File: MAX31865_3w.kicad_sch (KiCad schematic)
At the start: 6 parts, among them J1 Screw_Terminal_01x03, U3 MAX31865xAP

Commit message: Supprime le contour arduino qui fait plein d'erreur DRC
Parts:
- J1: footprint (none) -> TerminalBlock_Phoenix:TerminalBlock_Phoenix_MPT-0,5-3-2.54_1x03_P2.54mm_Horizontal
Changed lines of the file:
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@@
       (effects (font (size 1.27 1.27)) (justify left))
     )
-    (property "Footprint" "" (id 2) (at 212.09 90.17 0)
+    (property "Footprint" "TerminalBlock_Phoenix:TerminalBlock_Phoenix_MPT-0,5-3-2.54_1x03_P2.54mm_Horizontal" (id 2) (at 212.09 90.17 0)
       (effects (font (size 1.27 1.27)) hide)
     )

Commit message: 0 DRC
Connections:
- net DRDY: no longer names the net of U3.1 (~{DRDY})
- no-connect marks 0 -> 1
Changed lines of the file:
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@@
   (junction (at 144.78 100.33) (diameter 0) (color 0 0 0 0)
   )
+  (no_connect (at 74.93 72.39))
   (wire (pts (xy 120.65 55.88) (xy 120.65 48.26))
     (stroke (width 0) (type default) (color 0 0 0 0))
@@
   )
   (wire (pts (xy 124.46 114.3) (xy 124.46 118.11))
-    (stroke (width 0) (type default) (color 0 0 0 0))
-  )
-  (wire (pts (xy 74.93 72.39) (xy 109.22 72.39))
     (stroke (width 0) (type default) (color 0 0 0 0))
   )
@@
     (stroke (width 0) (type default) (color 0 0 0 0))
   )
+  (wire (pts (xy 74.93 72.39) (xy 109.22 72.39))
+    (stroke (width 0) (type default) (color 0 0 0 0))
+  )
   (wire (pts (xy 128.27 55.88) (xy 133.35 55.88))
     (stroke (width 0) (type default) (color 0 0 0 0))
@@
     (stroke (width 0) (type default) (color 0 0 0 0))
   )
-  (hierarchical_label "DRDY" (shape output) (at 74.93 72.39 180)
-    (effects (font (size 1.27 1.27)) (justify right))
-  )
   (hierarchical_label "SCLK" (shape input) (at 74.93 77.47 180)

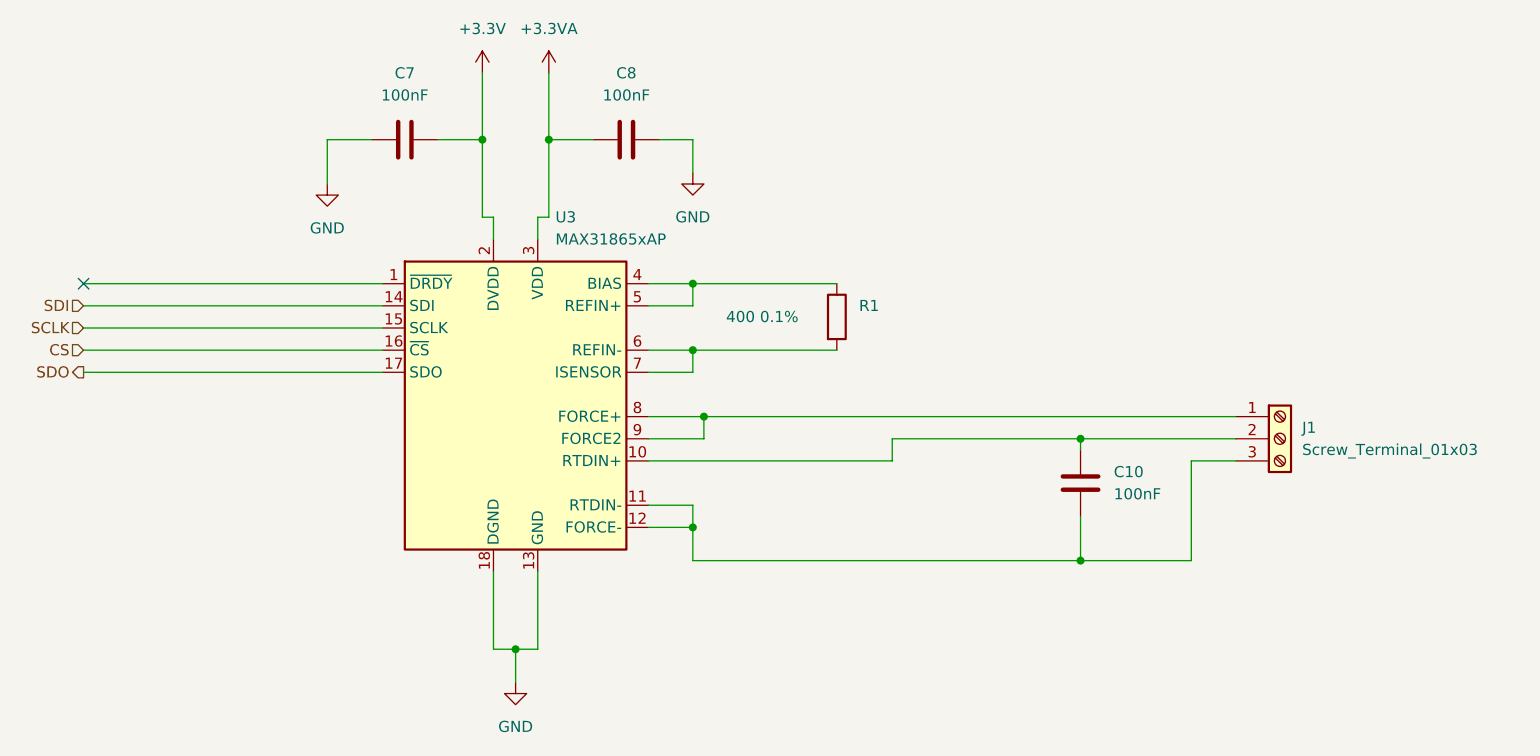
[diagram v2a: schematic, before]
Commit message: Passe l'empreinte en TSOP
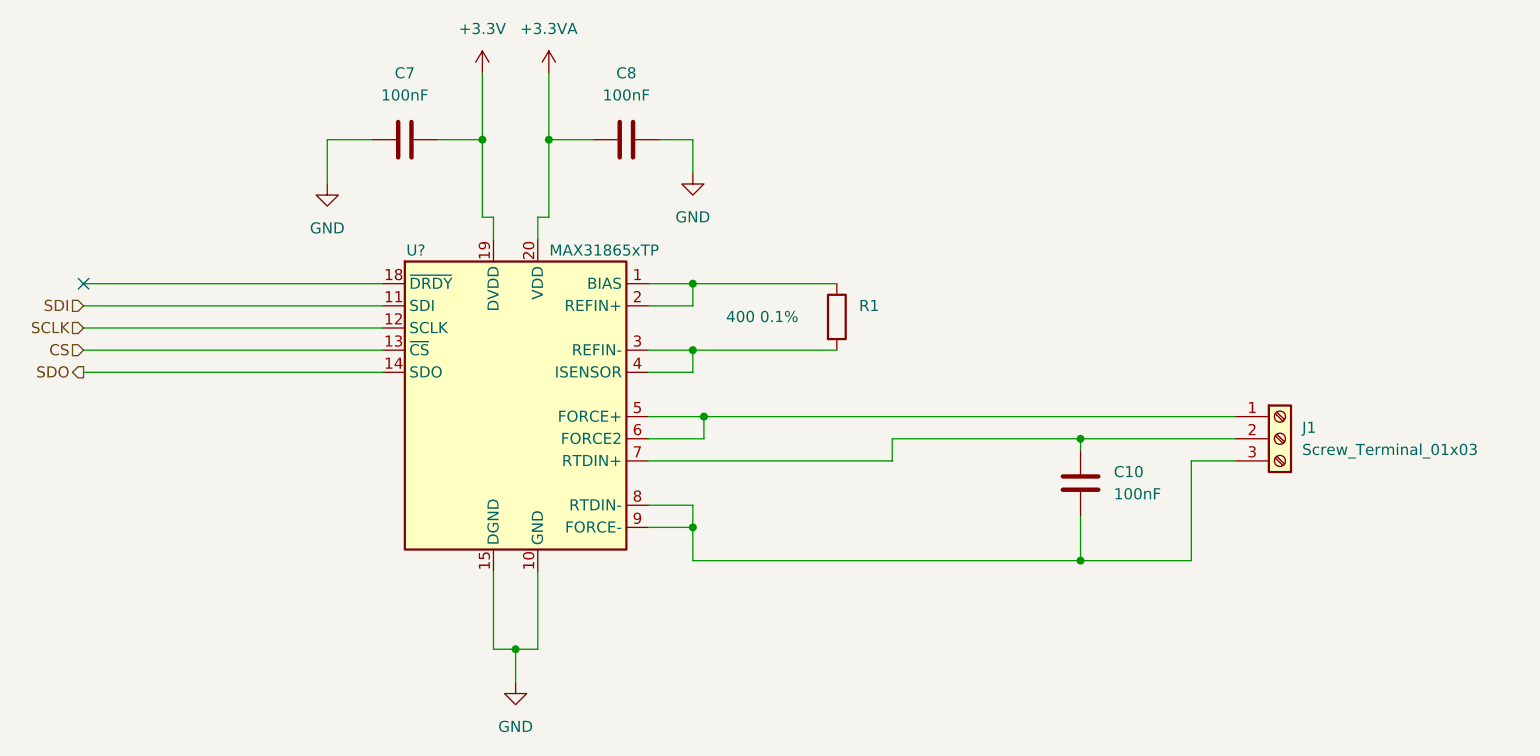
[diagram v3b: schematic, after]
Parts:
- U?: renamed from U3; value MAX31865xAP -> MAX31865xTP; footprint Package_SO:SSOP-20_5.3x7.2mm_P0.65mm -> Package_DFN_QFN:TQFN-20-1EP_5x5mm_P0.65mm_EP3.25x3.25mm; symbol Sensor_Temperature:MAX31865xAP -> Sensor_Temperature:MAX31865xTP
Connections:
- net +3.3V: now also U?.19 (DVDD); no longer U?.2 (DVDD)
- net +3.3VA: now also U?.20 (VDD); no longer U?.3 (VDD)
- net CS: now also U?.13 (~{CS}); no longer U?.16 (~{CS})
- net GND: now also U?.10 (GND), U?.15 (DGND), U?.16 (GND), U?.21 (GND); no longer U?.13 (GND), U?.18 (DGND), U?.19 (GND)
- net SCLK: now also U?.12 (SCLK); no longer U?.15 (SCLK)
- net SDI: now also U?.11 (SDI); no longer U?.14 (SDI)
- net SDO: now also U?.14 (SDO); no longer U?.17 (SDO)
- net at U?.1 (BIAS): now also R1.1, U?.2 (REFIN+)
- net at C10.2, J1.2 (Pin_2): now also U?.7 (RTDIN+); no longer U?.10 (RTDIN+)
- net at C10.1, J1.3 (Pin_3): now also U?.8 (RTDIN-), U?.9 (FORCE-); no longer U?.11 (RTDIN-), U?.12 (FORCE-)
- new net: R1.2, U?.3 (REFIN-), U?.4 (ISENSOR)
- new net: J1.1 (Pin_1), U?.5 (FORCE+), U?.6 (FORCE2)
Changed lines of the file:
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@@
     (effects (font (size 1.27 1.27)) (justify right))
   )
-  (symbol (lib_id "Sensor_Temperature:MAX31865xAP") (at 124.46 87.63 0) (unit 1)
+  (symbol (lib_id "Sensor_Temperature:MAX31865xTP") (at 124.46 87.63 0) (unit 1)
     (in_bom yes) (on_board yes) (fields_autoplaced)
-    (property "Reference" "U3" (id 0) (at 129.0194 64.77 0)
-      (effects (font (size 1.27 1.27)) (justify left))
-    )
-    (property "Value" "MAX31865xAP" (id 1) (at 129.0194 67.31 0)
-      (effects (font (size 1.27 1.27)) (justify left))
-    )
-    (property "Footprint" "Package_SO:SSOP-20_5.3x7.2mm_P0.65mm" (id 2) (at 128.27 104.14 0)
+    (property "Reference" "U?" (id 0) (at 113.03 68.58 0))
+    (property "Value" "MAX31865xTP" (id 1) (at 134.62 68.58 0))
+    (property "Footprint" "Package_DFN_QFN:TQFN-20-1EP_5x5mm_P0.65mm_EP3.25x3.25mm" (id 2) (at 128.27 104.14 0)
       (effects (font (size 1.27 1.27)) (justify left) hide)
     )
@@
     (pin "2")
     (pin "20")
+    (pin "21")
     (pin "3")
     (pin "4")

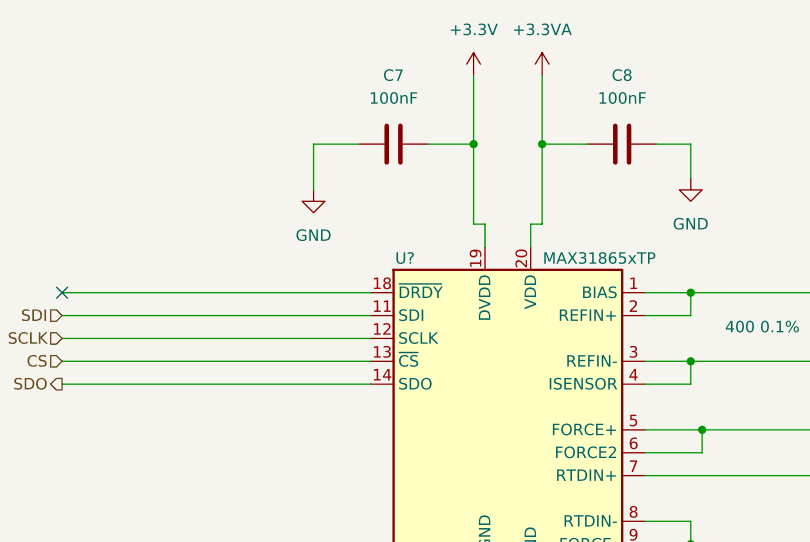
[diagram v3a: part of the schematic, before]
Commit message: Passe l'empreinte en TSOP
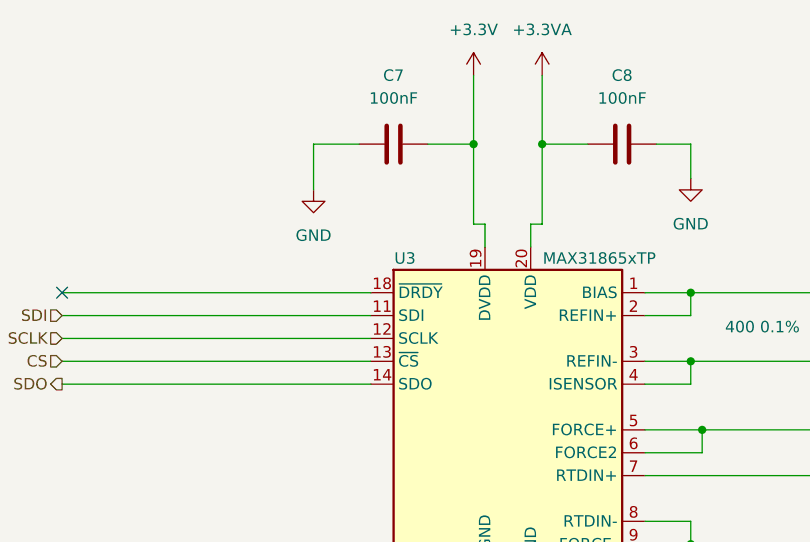
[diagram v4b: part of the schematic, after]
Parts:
- gave numbers to parts that had none: 1
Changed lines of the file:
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@@
   (symbol (lib_id "Sensor_Temperature:MAX31865xTP") (at 124.46 87.63 0) (unit 1)
     (in_bom yes) (on_board yes) (fields_autoplaced)
-    (property "Reference" "U?" (id 0) (at 113.03 68.58 0))
+    (property "Reference" "U3" (id 0) (at 113.03 68.58 0))
     (property "Value" "MAX31865xTP" (id 1) (at 134.62 68.58 0))
     (property "Footprint" "Package_DFN_QFN:TQFN-20-1EP_5x5mm_P0.65mm_EP3.25x3.25mm" (id 2) (at 128.27 104.14 0)

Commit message: Passe certaine empreinte en 0603
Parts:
- C10, C7, C8: footprint Capacitor_SMD:C_0805_2012Metric_Pad1.18x1.45mm_HandSolder -> Capacitor_SMD:C_0603_1608Metric_Pad1.08x0.95mm_HandSolder
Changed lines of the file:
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@@
     (property "Reference" "C7" (id 0) (at 111.76 48.26 90))
     (property "Value" "100nF" (id 1) (at 111.76 50.8 90))
-    (property "Footprint" "Capacitor_SMD:C_0805_2012Metric_Pad1.18x1.45mm_HandSolder" (id 2) (at 115.57 54.9148 0)
+    (property "Footprint" "Capacitor_SMD:C_0603_1608Metric_Pad1.08x0.95mm_HandSolder" (id 2) (at 115.57 54.9148 0)
       (effects (font (size 1.27 1.27)) hide)
     )
@@
     (property "Reference" "C8" (id 0) (at 137.16 48.26 90))
     (property "Value" "100nF" (id 1) (at 137.16 50.8 90))
-    (property "Footprint" "Capacitor_SMD:C_0805_2012Metric_Pad1.18x1.45mm_HandSolder" (id 2) (at 140.97 54.9148 0)
+    (property "Footprint" "Capacitor_SMD:C_0603_1608Metric_Pad1.08x0.95mm_HandSolder" (id 2) (at 140.97 54.9148 0)
       (effects (font (size 1.27 1.27)) hide)
     )
@@
       (effects (font (size 1.27 1.27)) (justify right))
     )
-    (property "Footprint" "Capacitor_SMD:C_0805_2012Metric_Pad1.18x1.45mm_HandSolder" (id 2) (at 188.2648 91.44 0)
+    (property "Footprint" "Capacitor_SMD:C_0603_1608Metric_Pad1.08x0.95mm_HandSolder" (id 2) (at 188.2648 91.44 0)
       (effects (font (size 1.27 1.27)) hide)
     )

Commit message: Passe les resistance 400 ohm en 1206
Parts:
- R1: footprint Resistor_SMD:R_0805_2012Metric_Pad1.20x1.40mm_HandSolder -> Resistor_SMD:R_1206_3216Metric_Pad1.30x1.75mm_HandSolder
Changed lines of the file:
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@@
       (effects (font (size 1.27 1.27)) (justify left))
     )
-    (property "Footprint" "Resistor_SMD:R_0805_2012Metric_Pad1.20x1.40mm_HandSolder" (id 2) (at 159.512 76.2 90)
+    (property "Footprint" "Resistor_SMD:R_1206_3216Metric_Pad1.30x1.75mm_HandSolder" (id 2) (at 159.512 76.2 90)
       (effects (font (size 1.27 1.27)) hide)
     )

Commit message: Ajoute selection 4w/3w Ajoute marquage v002
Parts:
- removed J1: Screw_Terminal_01x03, TerminalBlock_Phoenix:TerminalBlock_Phoenix_MPT-0,5-3-2.54_1x03_P2.54mm_Horizontal, symbol Connector:Screw_Terminal_01x03
- added J1: Screw_Terminal_01x04, TerminalBlock_Phoenix:TerminalBlock_Phoenix_MPT-0,5-4-2.54_1x04_P2.54mm_Horizontal, symbol Connector:Screw_Terminal_01x04
- added JP13, JP14: SolderJumper_3_Open, Jumper:SolderJumper-3_P1.3mm_Open_RoundedPad1.0x1.5mm_NumberLabels, symbol Jumper:SolderJumper_3_Open
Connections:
- net GND: now also JP13.3 (B)
- net at U3.5 (FORCE+): now also J1.1 (Pin_1), JP13.1 (A); no longer U3.6 (FORCE2)
- net at C10.2, U3.7 (RTDIN+): now also J1.2 (Pin_2)
- net at C10.1, U3.8 (RTDIN-): now also J1.3 (Pin_3), JP14.1 (A); no longer U3.9 (FORCE-)
- new net: JP13.2 (C), U3.6 (FORCE2)
- new net: JP14.2 (C), U3.9 (FORCE-)
- new net: J1.4 (Pin_4), JP14.3 (B)
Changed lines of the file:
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@@
   (junction (at 144.78 72.39) (diameter 0) (color 0 0 0 0)
   )
+  (junction (at 189.23 104.14) (diameter 0) (color 0 0 0 0)
+  )
   (junction (at 144.78 80.01) (diameter 0) (color 0 0 0 0)
   )
-  (junction (at 189.23 104.14) (diameter 0) (color 0 0 0 0)
+  (junction (at 142.24 87.63) (diameter 0) (color 0 0 0 0)
   )
   (junction (at 124.46 114.3) (diameter 0) (color 0 0 0 0)
   )
-  (junction (at 146.05 87.63) (diameter 0) (color 0 0 0 0)
-  )
   (junction (at 189.23 90.17) (diameter 0) (color 0 0 0 0)
   )
-  (junction (at 144.78 100.33) (diameter 0) (color 0 0 0 0)
+  (junction (at 147.32 97.79) (diameter 0) (color 0 0 0 0)
   )
   (no_connect (at 74.93 72.39))
@@
     (stroke (width 0) (type default) (color 0 0 0 0))
   )
-  (wire (pts (xy 146.05 87.63) (xy 146.05 90.17))
-    (stroke (width 0) (type default) (color 0 0 0 0))
-  )
-  (wire (pts (xy 146.05 87.63) (xy 207.01 87.63))
-    (stroke (width 0) (type default) (color 0 0 0 0))
-  )
   (wire (pts (xy 189.23 104.14) (xy 201.93 104.14))
     (stroke (width 0) (type default) (color 0 0 0 0))
   )
-  (wire (pts (xy 139.7 87.63) (xy 146.05 87.63))
+  (wire (pts (xy 147.32 95.25) (xy 147.32 97.79))
     (stroke (width 0) (type default) (color 0 0 0 0))
   )
@@
     (stroke (width 0) (type default) (color 0 0 0 0))
   )
+  (wire (pts (xy 147.32 104.14) (xy 189.23 104.14))
+    (stroke (width 0) (type default) (color 0 0 0 0))
+  )
   (wire (pts (xy 121.92 114.3) (xy 124.46 114.3))
     (stroke (width 0) (type default) (color 0 0 0 0))
@@
     (stroke (width 0) (type default) (color 0 0 0 0))
   )
+  (wire (pts (xy 139.7 100.33) (xy 149.86 100.33))
+    (stroke (width 0) (type default) (color 0 0 0 0))
+  )
+  (wire (pts (xy 144.78 85.09) (xy 142.24 85.09))
+    (stroke (width 0) (type default) (color 0 0 0 0))
+  )
   (wire (pts (xy 128.27 48.26) (xy 128.27 55.88))
     (stroke (width 0) (type default) (color 0 0 0 0))
   )
+  (wire (pts (xy 204.47 95.25) (xy 207.01 95.25))
+    (stroke (width 0) (type default) (color 0 0 0 0))
+  )
   (wire (pts (xy 167.64 92.71) (xy 167.64 90.17))
     (stroke (width 0) (type default) (color 0 0 0 0))
   )
+  (wire (pts (xy 147.32 95.25) (xy 153.67 95.25))
+    (stroke (width 0) (type default) (color 0 0 0 0))
+  )
   (wire (pts (xy 74.93 77.47) (xy 109.22 77.47))
     (stroke (width 0) (type default) (color 0 0 0 0))
@@
     (stroke (width 0) (type default) (color 0 0 0 0))
   )
-  (wire (pts (xy 139.7 90.17) (xy 146.05 90.17))
+  (wire (pts (xy 139.7 87.63) (xy 142.24 87.63))
     (stroke (width 0) (type default) (color 0 0 0 0))
   )
@@
     (stroke (width 0) (type default) (color 0 0 0 0))
   )
-  (wire (pts (xy 144.78 100.33) (xy 144.78 104.14))
+  (wire (pts (xy 142.24 85.09) (xy 142.24 87.63))
     (stroke (width 0) (type default) (color 0 0 0 0))
   )
@@
     (stroke (width 0) (type default) (color 0 0 0 0))
   )
-  (wire (pts (xy 139.7 97.79) (xy 144.78 97.79))
+  (wire (pts (xy 153.67 107.95) (xy 204.47 107.95))
+    (stroke (width 0) (type default) (color 0 0 0 0))
+  )
+  (wire (pts (xy 139.7 97.79) (xy 147.32 97.79))
     (stroke (width 0) (type default) (color 0 0 0 0))
   )
@@
     (stroke (width 0) (type default) (color 0 0 0 0))
   )
-  (wire (pts (xy 144.78 97.79) (xy 144.78 100.33))
+  (wire (pts (xy 142.24 87.63) (xy 207.01 87.63))
     (stroke (width 0) (type default) (color 0 0 0 0))
   )
@@
     (stroke (width 0) (type default) (color 0 0 0 0))
   )
-  (wire (pts (xy 139.7 100.33) (xy 144.78 100.33))
-    (stroke (width 0) (type default) (color 0 0 0 0))
-  )
   (wire (pts (xy 115.57 55.88) (xy 120.65 55.88))
     (stroke (width 0) (type default) (color 0 0 0 0))
@@
     (stroke (width 0) (type default) (color 0 0 0 0))
   )
+  (wire (pts (xy 147.32 97.79) (xy 147.32 104.14))
+    (stroke (width 0) (type default) (color 0 0 0 0))
+  )
   (wire (pts (xy 139.7 80.01) (xy 144.78 80.01))
     (stroke (width 0) (type default) (color 0 0 0 0))
   )
+  (wire (pts (xy 144.78 95.25) (xy 144.78 118.11))
+    (stroke (width 0) (type default) (color 0 0 0 0))
+  )
   (wire (pts (xy 127 64.77) (xy 128.27 64.77))
     (stroke (width 0) (type default) (color 0 0 0 0))
   )
+  (wire (pts (xy 204.47 107.95) (xy 204.47 95.25))
+    (stroke (width 0) (type default) (color 0 0 0 0))
+  )
   (wire (pts (xy 140.97 55.88) (xy 144.78 55.88))
     (stroke (width 0) (type default) (color 0 0 0 0))
@@
     (stroke (width 0) (type default) (color 0 0 0 0))
   )
-  (wire (pts (xy 144.78 104.14) (xy 189.23 104.14))
-    (stroke (width 0) (type default) (color 0 0 0 0))
-  )
   (wire (pts (xy 127 114.3) (xy 124.46 114.3))
     (stroke (width 0) (type default) (color 0 0 0 0))
@@
   )
   (wire (pts (xy 102.87 55.88) (xy 102.87 60.96))
+    (stroke (width 0) (type default) (color 0 0 0 0))
+  )
+  (wire (pts (xy 139.7 90.17) (xy 140.97 90.17))
+    (stroke (width 0) (type default) (color 0 0 0 0))
+  )
+  (wire (pts (xy 153.67 105.41) (xy 153.67 107.95))
     (stroke (width 0) (type default) (color 0 0 0 0))
   )
@@
     (pin "1")
   )
-  (symbol (lib_id "Connector:Screw_Terminal_01x03") (at 212.09 90.17 0) (unit 1)
-    (in_bom yes) (on_board yes) (fields_autoplaced)
-    (property "Reference" "J1" (id 0) (at 214.63 88.8999 0)
-      (effects (font (size 1.27 1.27)) (justify left))
-    )
-    (property "Value" "Screw_Terminal_01x03" (id 1) (at 214.63 91.4399 0)
-      (effects (font (size 1.27 1.27)) (justify left))
-    )
-    (property "Footprint" "TerminalBlock_Phoenix:TerminalBlock_Phoenix_MPT-0,5-3-2.54_1x03_P2.54mm_Horizontal" (id 2) (at 212.09 90.17 0)
-      (effects (font (size 1.27 1.27)) hide)
-    )
-    (property "Datasheet" "~" (id 3) (at 212.09 90.17 0)
+  (symbol (lib_id "Jumper:SolderJumper_3_Open") (at 144.78 90.17 270) (unit 1)
+    (in_bom yes) (on_board yes) (fields_autoplaced)
+    (property "Reference" "JP13" (id 0) (at 147.32 88.8999 90)
+      (effects (font (size 1.27 1.27)) (justify left))
+    )
+    (property "Value" "SolderJumper_3_Open" (id 1) (at 147.32 91.4399 90)
+      (effects (font (size 1.27 1.27)) (justify left))
+    )
+    (property "Footprint" "Jumper:SolderJumper-3_P1.3mm_Open_RoundedPad1.0x1.5mm_NumberLabels" (id 2) (at 144.78 90.17 0)
+      (effects (font (size 1.27 1.27)) hide)
+    )
+    (property "Datasheet" "~" (id 3) (at 144.78 90.17 0)
       (effects (font (size 1.27 1.27)) hide)
     )
@@
     )
     (property "Datasheet" "" (id 3) (at 120.65 48.26 0)
+      (effects (font (size 1.27 1.27)) hide)
+    )
+    (pin "1")
+  )
+  (symbol (lib_id "Jumper:SolderJumper_3_Open") (at 153.67 100.33 270) (unit 1)
+    (in_bom yes) (on_board yes) (fields_autoplaced)
+    (property "Reference" "JP14" (id 0) (at 156.21 99.0599 90)
+      (effects (font (size 1.27 1.27)) (justify left))
+    )
+    (property "Value" "SolderJumper_3_Open" (id 1) (at 156.21 101.5999 90)
+      (effects (font (size 1.27 1.27)) (justify left))
+    )
+    (property "Footprint" "Jumper:SolderJumper-3_P1.3mm_Open_RoundedPad1.0x1.5mm_NumberLabels" (id 2) (at 153.67 100.33 0)
+      (effects (font (size 1.27 1.27)) hide)
+    )
+    (property "Datasheet" "~" (id 3) (at 153.67 100.33 0)
+      (effects (font (size 1.27 1.27)) hide)
+    )
+    (pin "1")
+    (pin "2")
+    (pin "3")
+  )
+  (symbol (lib_name "GND_1") (lib_id "power:GND") (at 144.78 118.11 0) (unit 1)
+    (in_bom yes) (on_board yes) (fields_autoplaced)
+    (property "Reference" "#PWR036" (id 0) (at 144.78 124.46 0)
+      (effects (font (size 1.27 1.27)) hide)
+    )
+    (property "Value" "GND" (id 1) (at 144.78 123.19 0))
+    (property "Footprint" "" (id 2) (at 144.78 118.11 0)
+      (effects (font (size 1.27 1.27)) hide)
+    )
+    (property "Datasheet" "" (id 3) (at 144.78 118.11 0)
       (effects (font (size 1.27 1.27)) hide)
     )
@@
     (pin "2")
   )
+  (symbol (lib_id "Connector:Screw_Terminal_01x04") (at 212.09 90.17 0) (unit 1)
+    (in_bom yes) (on_board yes) (fields_autoplaced)
+    (property "Reference" "J1" (id 0) (at 214.63 90.1699 0)
+      (effects (font (size 1.27 1.27)) (justify left))
+    )
+    (property "Value" "Screw_Terminal_01x04" (id 1) (at 214.63 92.7099 0)
+      (effects (font (size 1.27 1.27)) (justify left))
+    )
+    (property "Footprint" "TerminalBlock_Phoenix:TerminalBlock_Phoenix_MPT-0,5-4-2.54_1x04_P2.54mm_Horizontal" (id 2) (at 212.09 90.17 0)
+      (effects (font (size 1.27 1.27)) hide)
+    )
+    (property "Datasheet" "~" (id 3) (at 212.09 90.17 0)
+      (effects (font (size 1.27 1.27)) hide)
+    )
+    (pin "1")
+    (pin "2")
+    (pin "3")
+    (pin "4")
+  )
   (symbol (lib_id "power:GND") (at 102.87 60.96 0) (unit 1)
